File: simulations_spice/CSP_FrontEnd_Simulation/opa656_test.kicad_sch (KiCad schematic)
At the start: 8 parts, among them X1 opa656

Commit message: Output_Updation
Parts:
- added Cf2, Cs1: 100p, symbol Device:C
- added Rf2: 10k, symbol eSim_Devices:resistor
- added Rpz1: 500k, symbol eSim_Devices:resistor
- added X2: opa656, symbol eSim_Subckt:opa656
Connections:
- net GND: now also X2.1 (IN_PLUS)
- net vout: now also Cs1.1, Rpz1.2
- net at X1.4 (VEE), v3.2 (-): now also X2.4 (VEE)
- net at X1.3 (VCC), v2.1 (+): now also X2.3 (VCC)
- new net: Cf2.1, Cs1.2, Rf2.2, Rpz1.1, X2.2 (IN_MINUS)
- new net Shaped_Out: Cf2.2, Rf2.1, X2.5 (OUT)

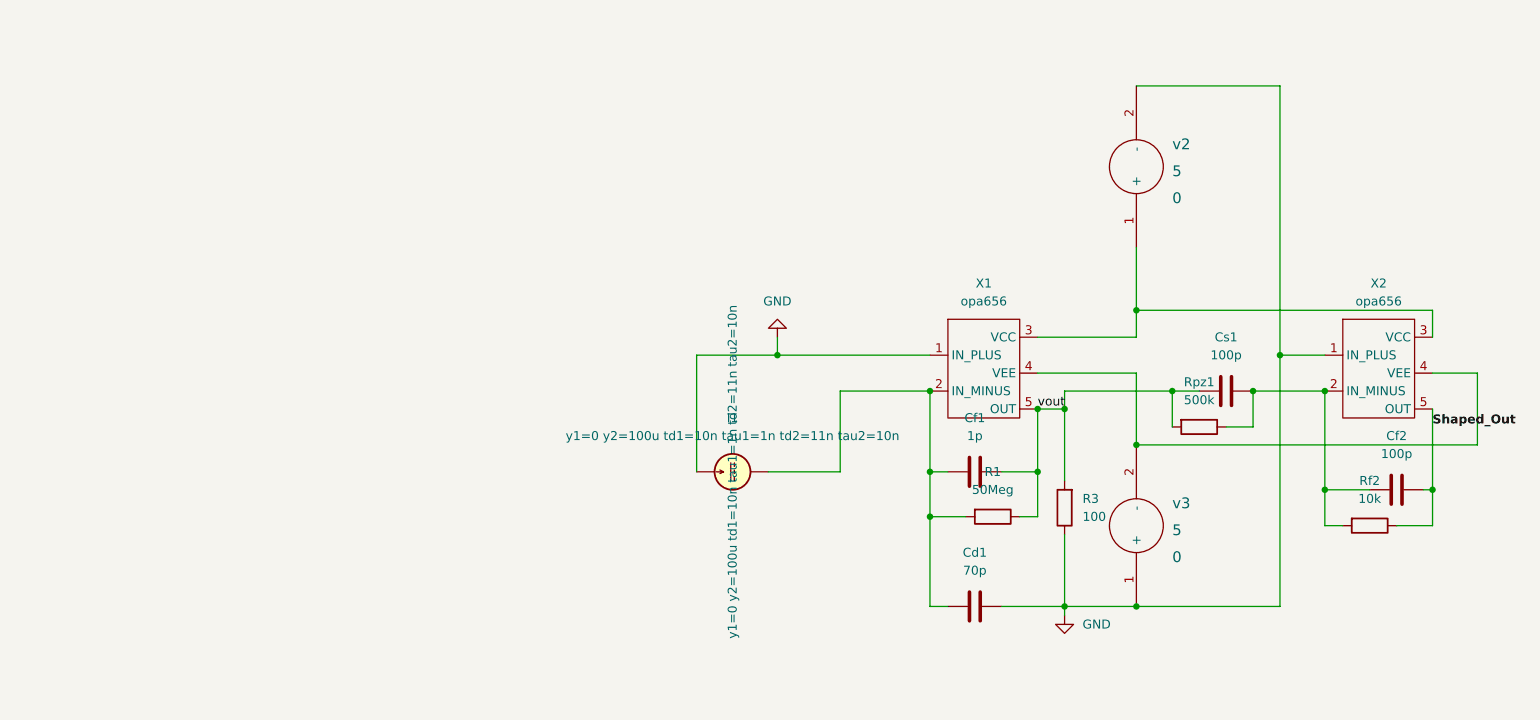
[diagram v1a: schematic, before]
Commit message: complete phase 1 mixed-signal simulation and behavioral modeling
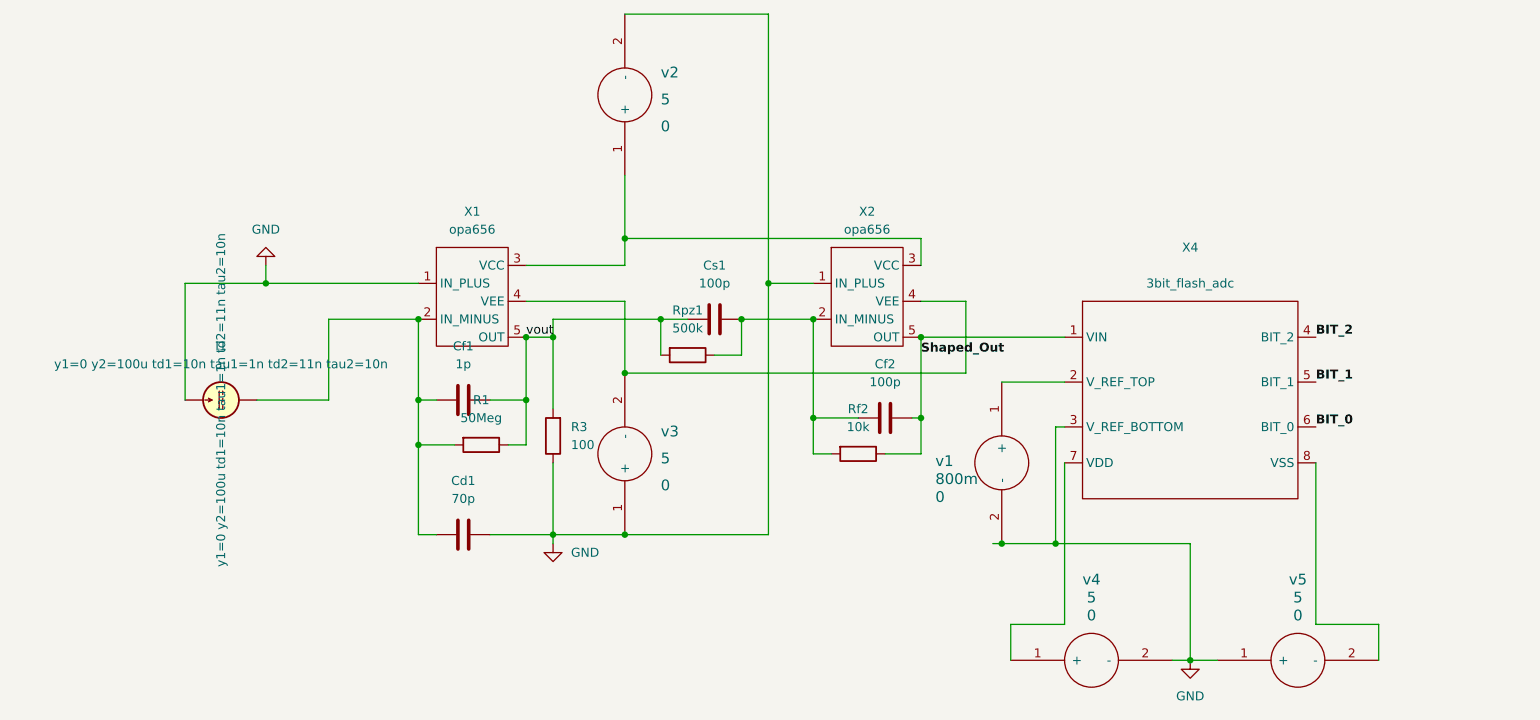
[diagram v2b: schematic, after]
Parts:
- added X4: ~, symbol OpenDAQ_Custom:ADC_3BIT_FLASH
- added v1: 800m, 0, symbol eSim_Sources:DC
- added v4, v5: 5, 0, symbol eSim_Sources:DC
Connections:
- net GND: now also X4.3 (V_REF_BOTTOM), v1.2 (-), v4.2 (-), v5.1 (+)
- net Shaped_Out: now also X4.1 (VIN)
- new net: X4.7 (VDD), v4.1 (+)
- new net: X4.8 (VSS), v5.2 (-)
- new net: X4.2 (V_REF_TOP), v1.1 (+)
- new net BIT_0: X4.6 (BIT_0)
- new net BIT_1: X4.5 (BIT_1)
- new net BIT_2: X4.4 (BIT_2)
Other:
- moved on the sheet: Cd1, Cf1, Cf2, Cs1, I1, R1, R3, Rf2, Rpz1, X1, X2, v2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
